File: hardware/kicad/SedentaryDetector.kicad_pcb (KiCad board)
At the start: 2 copper layers, 50 x 35 mm, 2 parts, among them J1 ESP32-C3_2x9, J2 MPU6050_1x8

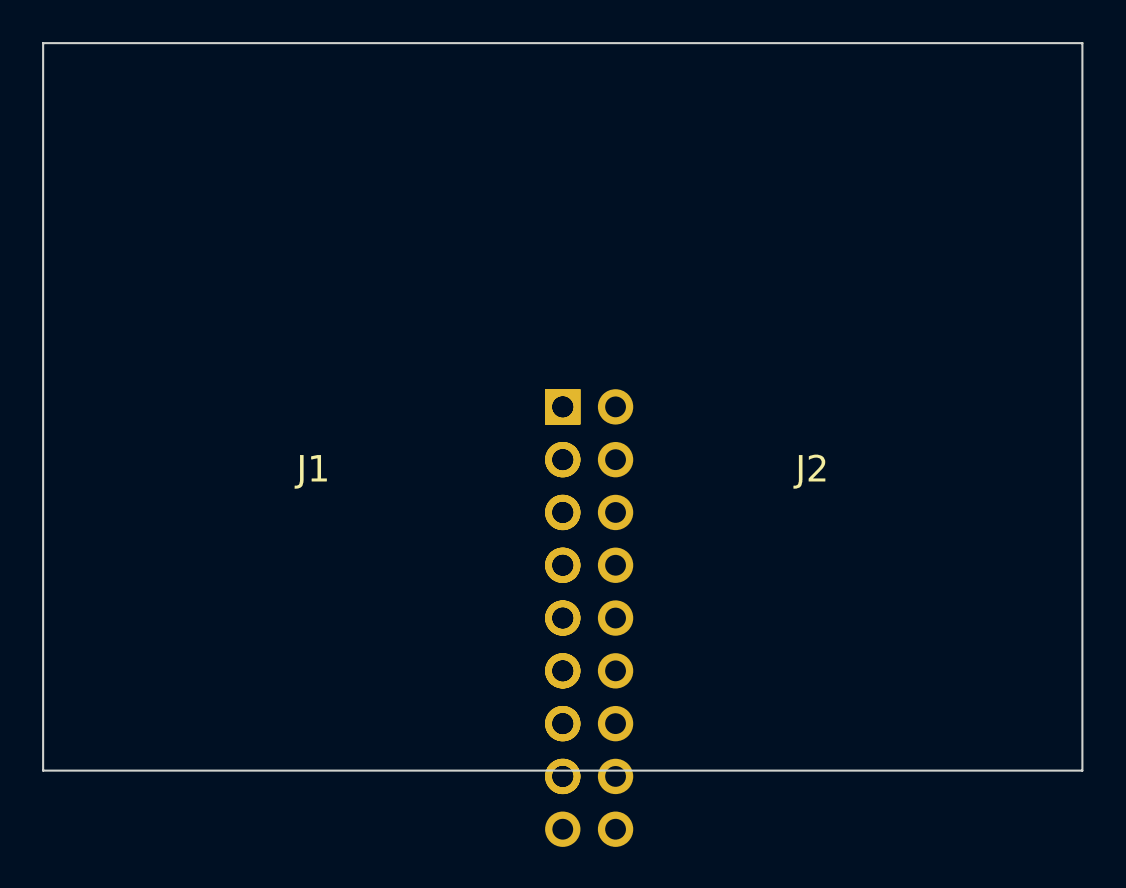
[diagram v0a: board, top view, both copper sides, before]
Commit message: feat(hardware): regenerate PCB with KiCad 10 pcbnew API
Use KiCad 10 system pcbnew API (via kicad-python wrapper):
- Board: 50x35mm, 2-layer, 1.6mm (KiCad 10 format)
- J1: ESP32-C3 2x9 (PinSocket, THT pads)
- J2: MPU6050 1x8 (PinSocket, THT pads)
- GND copper pour on B.Cu layer
- Net declarations for all ESP32 + MPU6050 pins

Workflow: kicad-python Tools/gen_kicad_pcb.py
Verified: KiCad CLI SVG export OK
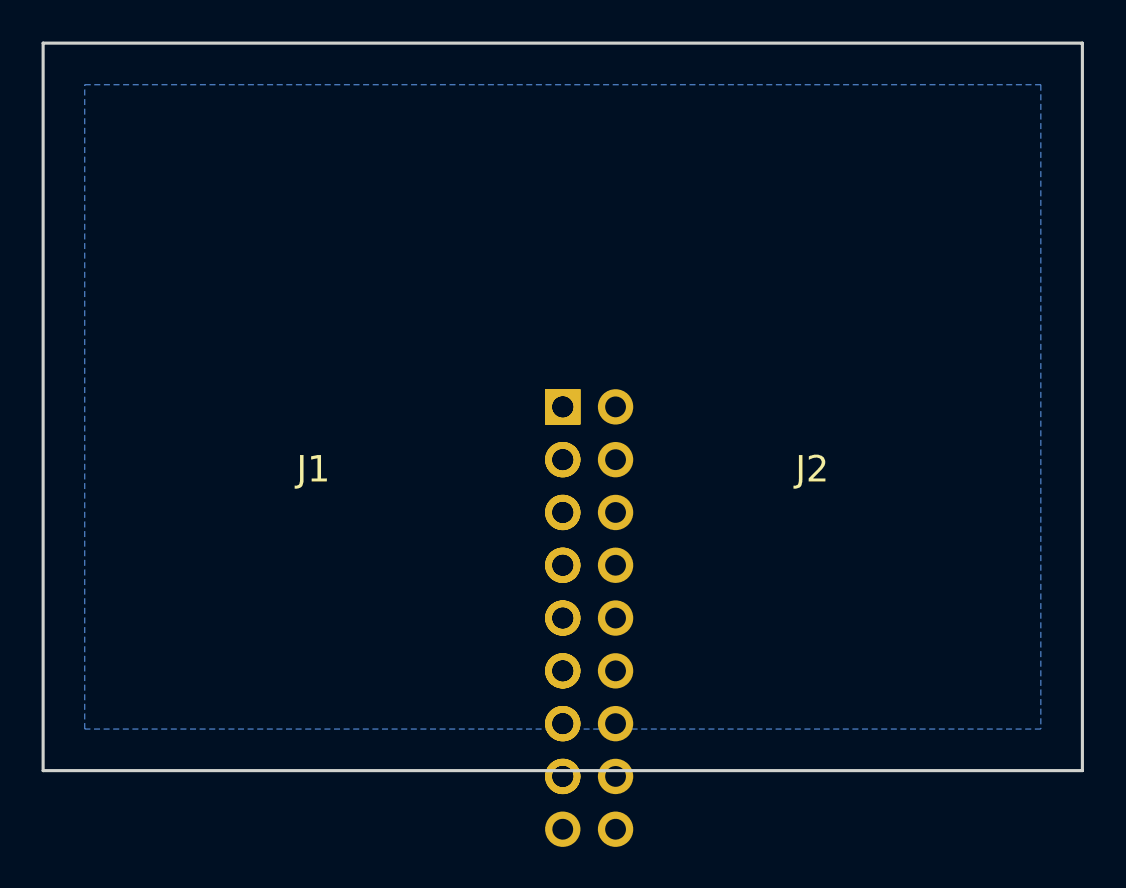
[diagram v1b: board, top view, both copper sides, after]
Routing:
- added copper zone on B.Cu, net GND
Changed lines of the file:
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@@
 	)
 	(paper "A4")
+	(title_block
+		(title "Sedentary Detector - Carrier Board")
+		(date "2026-06-20")
+		(rev "0.1")
+	)
 	(layers
 		(0 "F.Cu" signal)
@@
 		(end 25 -17.5)
 		(stroke
-			(width 0.1)
+			(width 0.15)
 			(type default)
 		)
@@
 		(end -25 -17.5)
 		(stroke
-			(width 0.1)
+			(width 0.15)
 			(type default)
 		)
@@
 		(end 25 17.5)
 		(stroke
-			(width 0.1)
+			(width 0.15)
 			(type default)
 		)
@@
 		(end -25 17.5)
 		(stroke
-			(width 0.1)
+			(width 0.15)
 			(type default)
 		)
 		(layer "Edge.Cuts")
 	)
+	(zone
+		(net "GND")
+		(layer "B.Cu")
+		(hatch edge 0.5)
+		(connect_pads yes
+			(clearance 0.5)
+		)
+		(min_thickness 0.25)
+		(fill
+			(thermal_gap 0.5)
+			(thermal_bridge_width 0.5)
+			(island_removal_mode 0)
+		)
+		(polygon
+			(pts
+				(xy -23 -15.5) (xy 23 -15.5) (xy 23 15.5) (xy -23 15.5)
+			)
+		)
+	)
 	(embedded_fonts no)

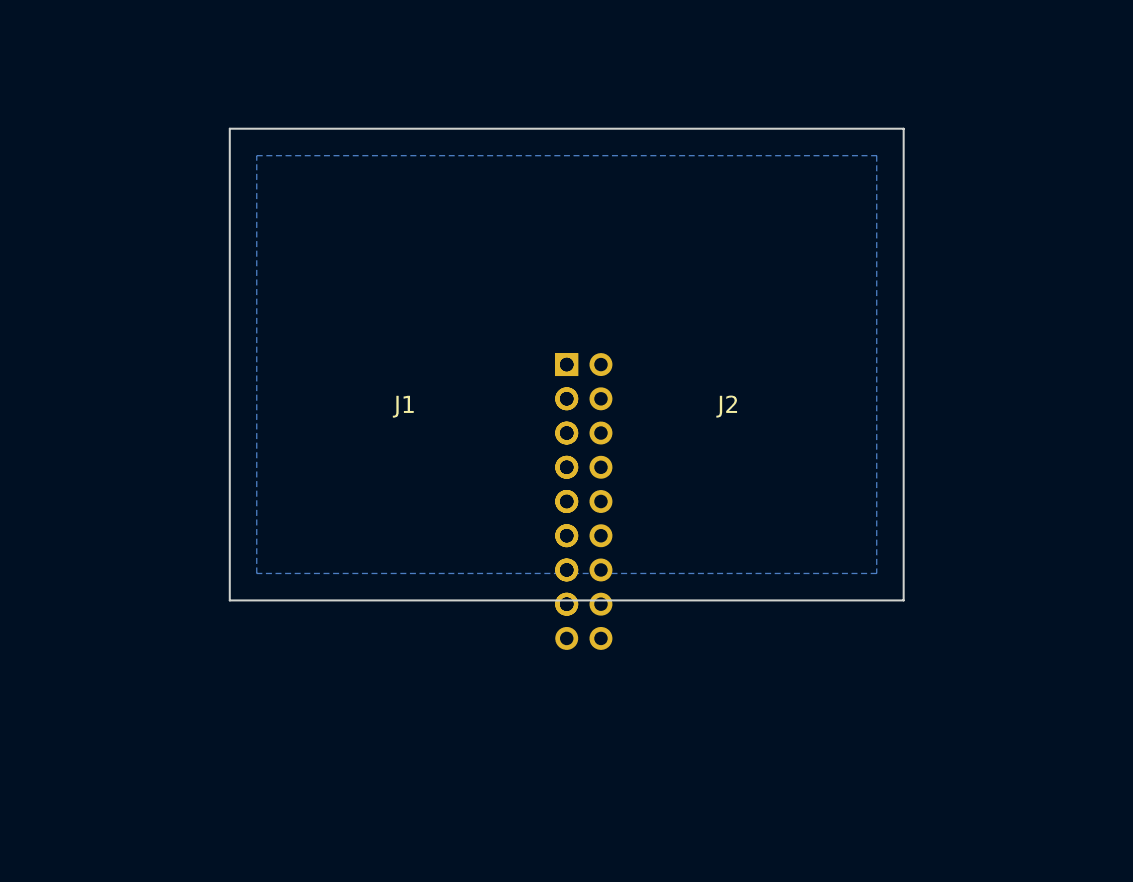
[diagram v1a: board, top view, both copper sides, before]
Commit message: feat(hardware): ESP32-WROOM-32 2x15 + MPU6050 1x8 PCB layout
PCB (KiCad 10 pcbnew API):
- Board: 80x50mm, centered layout
- J1: ESP32-WROOM-32 2x15 header @ (-30, -17.8)mm
- J2: MPU6050 GY-521 1x8 header @ (30, -7.6)mm
- GND copper pour on B.Cu
- M3 mounting holes at 4 corners
- Net assignments: GND, 3V3, I2C_SDA, I2C_SCL, MPU_INT, VIN_SW

Dimensions: 24.5mm row spacing, 2.54mm pin pitch
Schematics: in KiCad GUI (hand-writing S-expr format is error-prone)
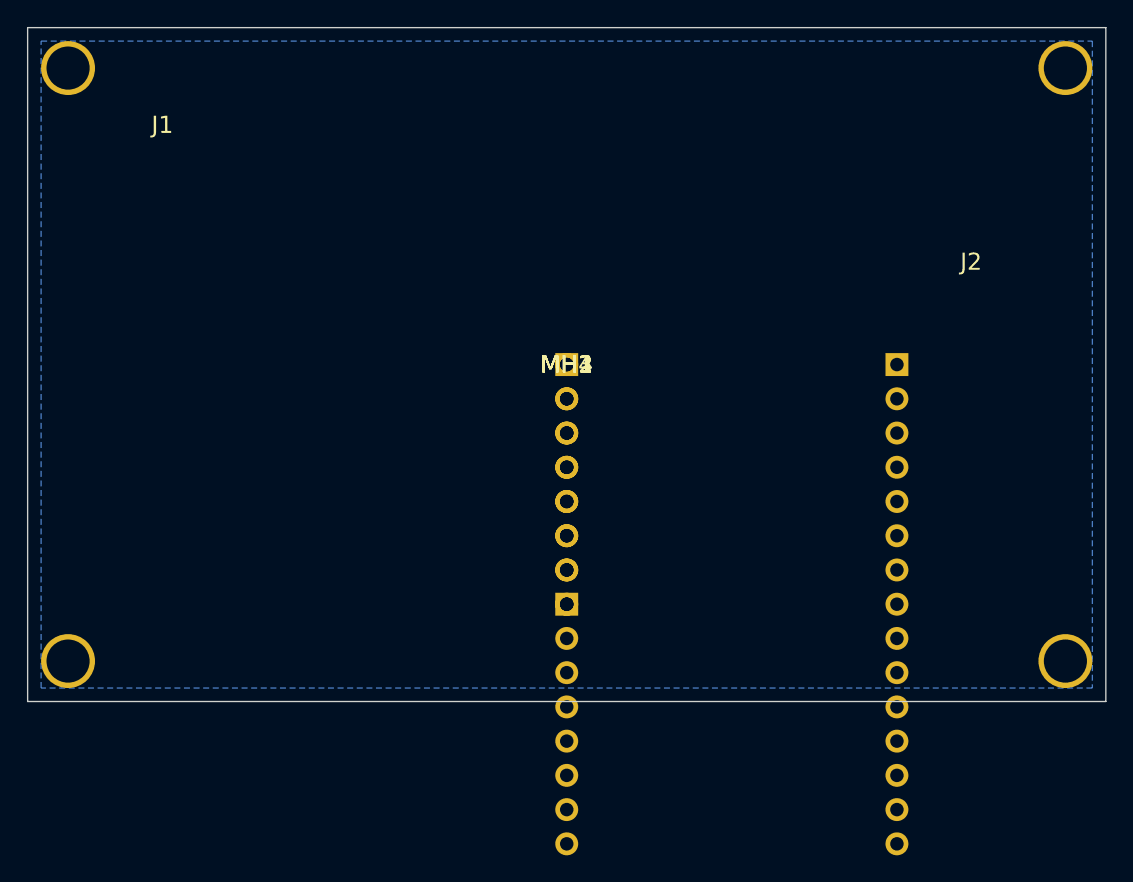
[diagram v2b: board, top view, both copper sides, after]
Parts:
- added MH1, MH2, MH3, MH4: , , F.Cu at (0.00, 0.00)
- J1: value ESP32-C3_2x9 -> ESP32-WROOM-32_2x15
- moved J1 27.5 mm to (-30.0, -17.8)
- moved J2 20.9 mm to (30.0, -7.62)
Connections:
- J1 pad 1: (no net) -> GND
- J1 pad 16: (no net) -> GND
- J1 pad 17: (no net) -> VIN_SW
- J1 pad 2: (no net) -> 3V3
- J1 pad 5: (no net) -> MPU_INT
- J1 pad 7: (no net) -> I2C_SDA
- J1 pad 8: (no net) -> I2C_SCL
- J2 pad 1: (no net) -> 3V3
- J2 pad 2: (no net) -> GND
- J2 pad 3: (no net) -> I2C_SCL
- J2 pad 4: (no net) -> I2C_SDA
- J2 pad 8: (no net) -> MPU_INT
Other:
- board size 50 x 35 mm -> 80 x 50 mm
